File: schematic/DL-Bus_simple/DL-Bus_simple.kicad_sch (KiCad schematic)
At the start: 4 parts, among them J1 DL-Bus, U1 esp32-wemos-d1-mini

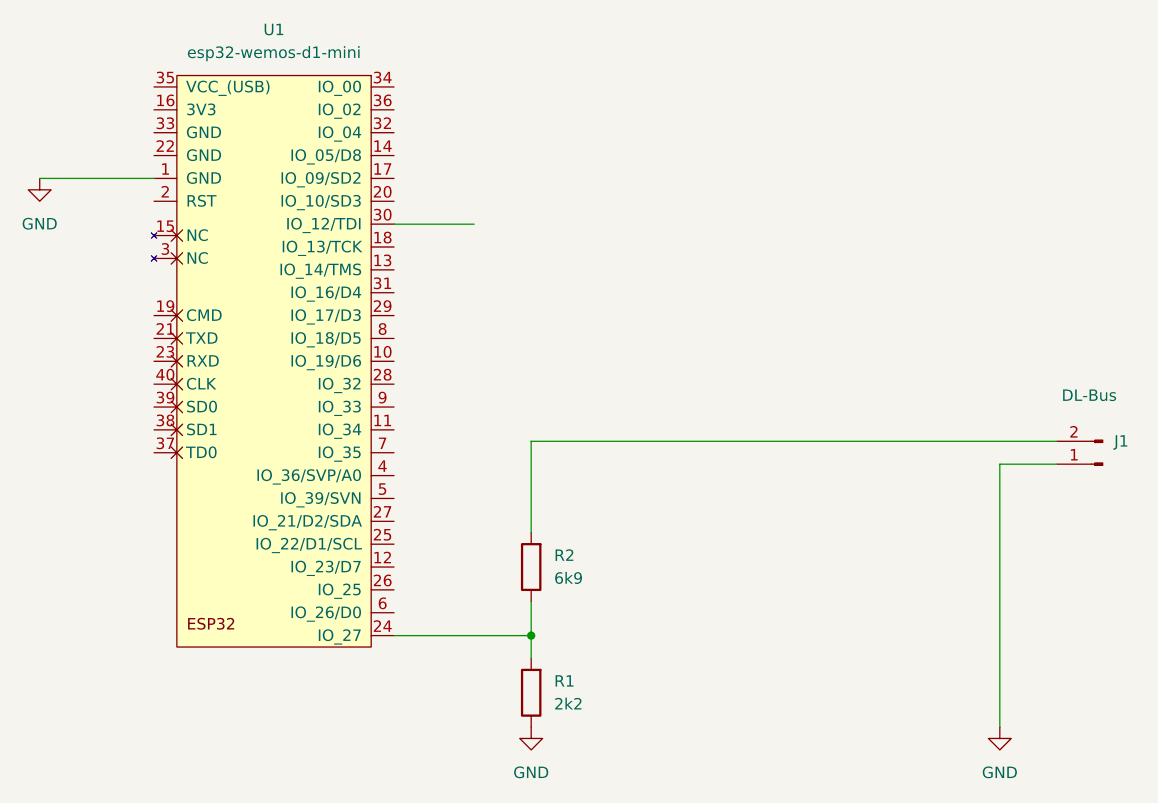
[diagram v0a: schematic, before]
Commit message: removed DebugPin remains
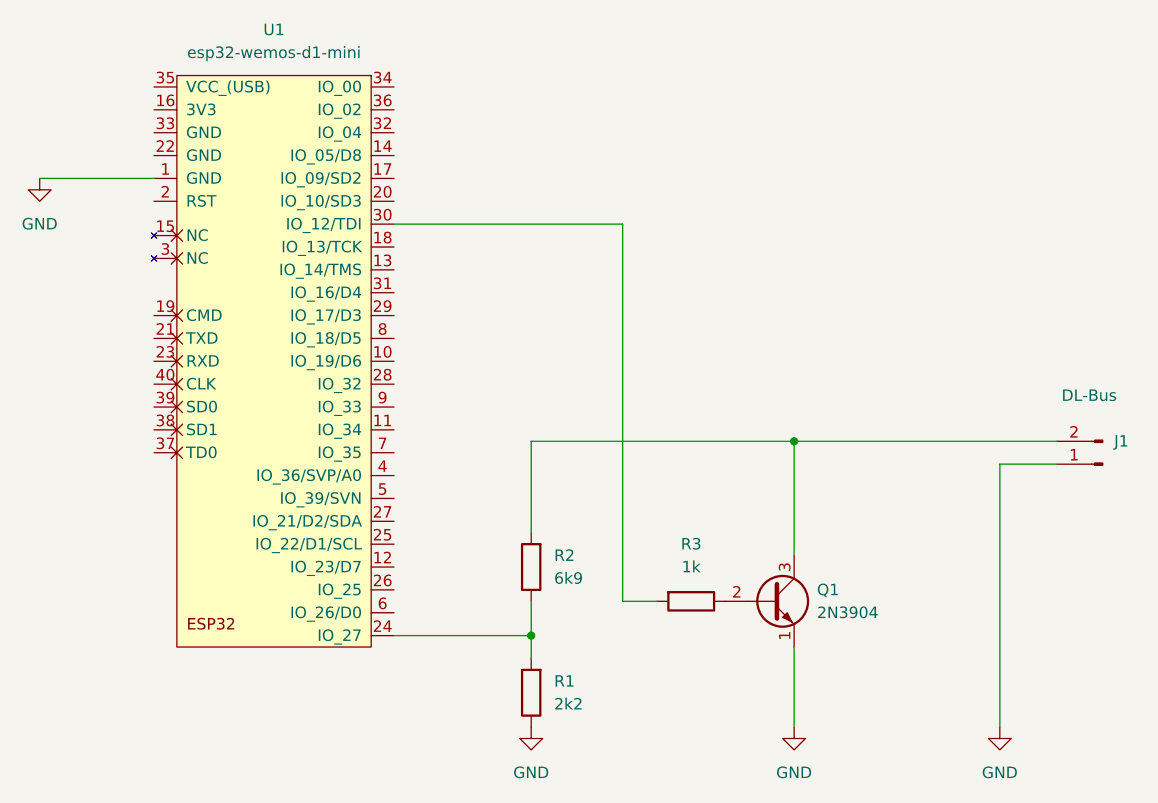
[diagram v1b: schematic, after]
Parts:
- added Q1: 2N3904, Package_TO_SOT_THT:TO-92_Inline, symbol Transistor_BJT:2N3904
- added R3: 1k, symbol Device:R
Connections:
- net GND: now also Q1.1 (E)
- net at U1.30 (IO_12/TDI): now also R3.2
- net at J1.2 (Pin_2), R2.2: now also Q1.3 (C)
- new net: Q1.2 (B), R3.1

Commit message: fix HW bug
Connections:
- net at U1.29 (IO_17/D3): now also R3.2
- net at U1.30 (IO_12/TDI): no longer R3.2
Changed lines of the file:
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@@
+	(wire
+		(pts
+			(xy 107.95 82.55) (xy 133.35 82.55)
+		)
+		(stroke
+			(width 0)
+			(type default)
+		)
+	)
 	(wire
 		(pts
@@
 	(wire
 		(pts
-			(xy 107.95 72.39) (xy 133.35 72.39)
+			(xy 133.35 114.3) (xy 133.35 82.55)
 		)
 		(stroke
-			(width 0)
-			(type default)
-		)
-	)
-	(wire
-		(pts
-			(xy 133.35 114.3) (xy 133.35 72.39)
-		)
-		(stroke
